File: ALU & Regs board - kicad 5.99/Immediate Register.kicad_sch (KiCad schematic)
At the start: 4 parts, among them U45 MC74ACT244DWG, U46 MC74ACT244DWG

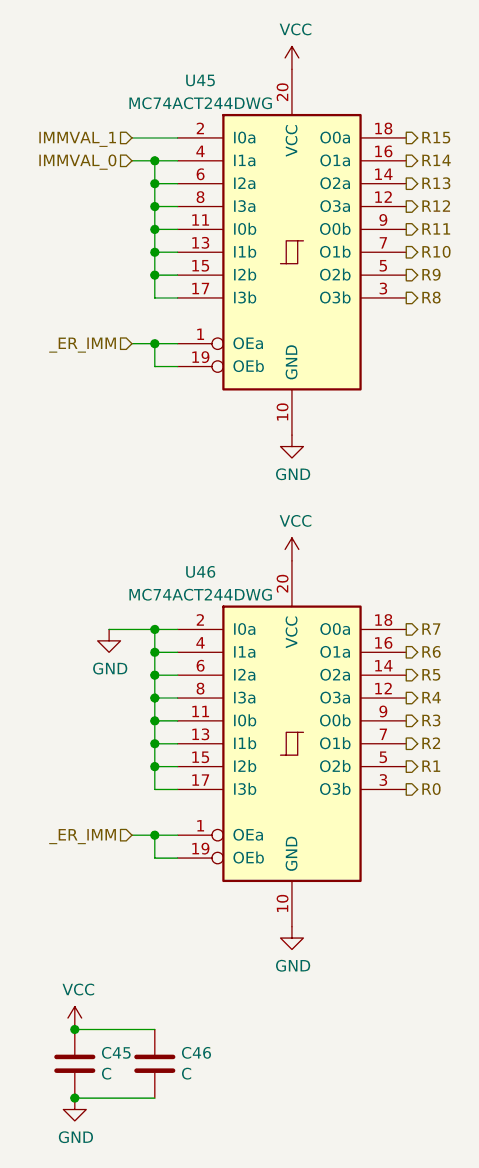
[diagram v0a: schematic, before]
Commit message: added a buffer on the _RESET line, which is rather loaded
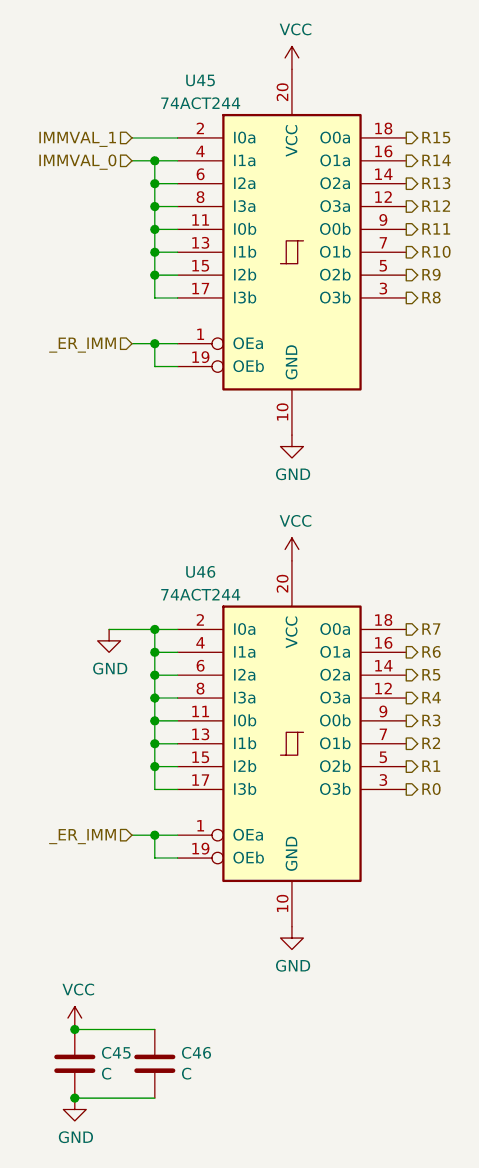
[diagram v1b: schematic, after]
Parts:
- U45, U46: value MC74ACT244DWG -> 74ACT244
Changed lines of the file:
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@@
     (in_bom yes) (on_board yes)
     (property "Reference" "U45" (id 0) (at 40.64 40.64 0))
-    (property "Value" "MC74ACT244DWG " (id 1) (at 40.64 43.18 0))
+    (property "Value" "74ACT244" (id 1) (at 40.64 43.18 0))
     (property "Footprint" "Package_SO:SOIC-20W_7.5x12.8mm_P1.27mm" (id 2) (at 50.8 59.69 0)
       (effects (font (size 1.27 1.27)) hide)
@@
     (in_bom yes) (on_board yes)
     (property "Reference" "U46" (id 0) (at 40.64 95.25 0))
-    (property "Value" "MC74ACT244DWG " (id 1) (at 40.64 97.79 0))
+    (property "Value" "74ACT244" (id 1) (at 40.64 97.79 0))
     (property "Footprint" "Package_SO:SOIC-20W_7.5x12.8mm_P1.27mm" (id 2) (at 50.8 114.3 0)
       (effects (font (size 1.27 1.27)) hide)
